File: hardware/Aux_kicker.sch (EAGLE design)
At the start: 23 parts, among them IC1 PIC18F4431S, IC2 MIC4429M, IC3 LM324D, Q1 IRF520

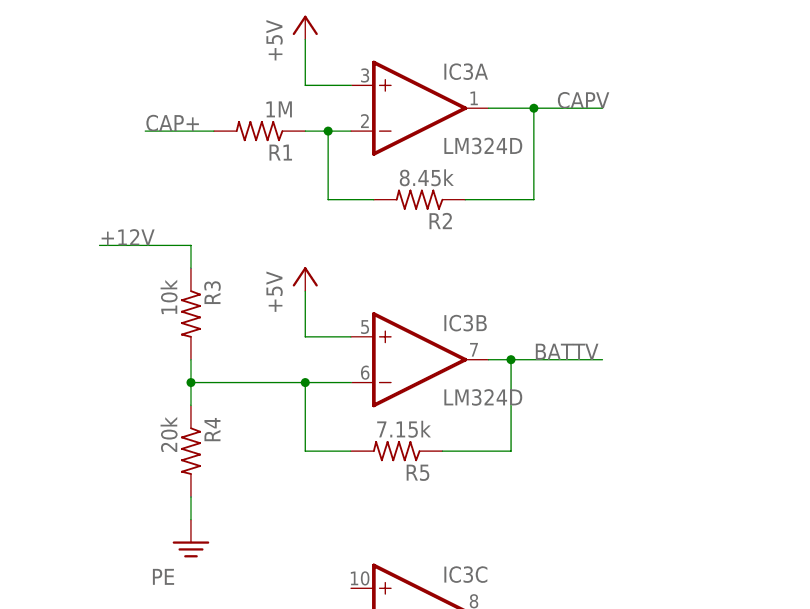
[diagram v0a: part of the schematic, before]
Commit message: Minor resistance value changes to aux kicker board
Changed values of resistances in op amp circuit to reflect ones used on
aux kicker boards with new 250V capacitors (instead of 500V capacitors)
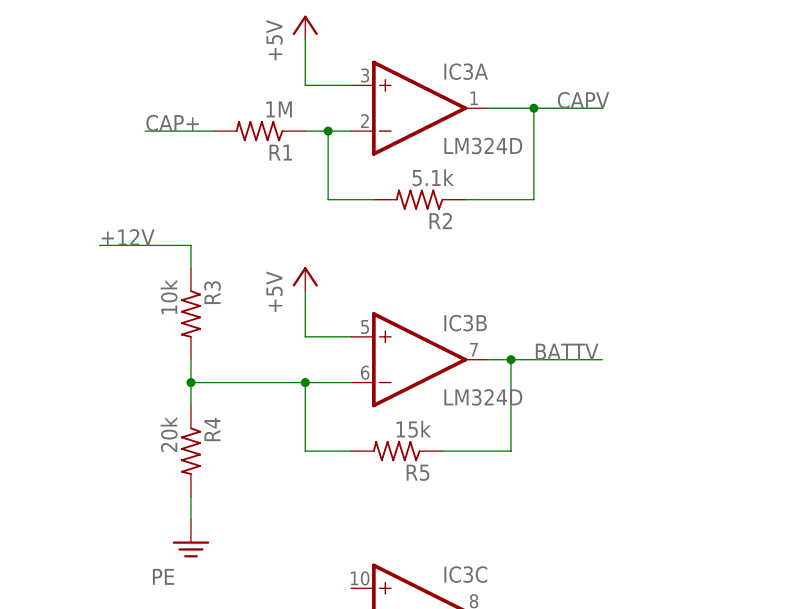
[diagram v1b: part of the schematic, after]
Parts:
- R2: value 8.45k -> 5.1k
- R5: value 7.15k -> 15k
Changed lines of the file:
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@@
 <part name="R1" library="rcl" deviceset="R-US_" device="R0805" value="1M"/>
 <part name="P+7" library="supply1" deviceset="+5V" device=""/>
-<part name="R2" library="rcl" deviceset="R-US_" device="R0805" value="8.45k"/>
+<part name="R2" library="rcl" deviceset="R-US_" device="R0805" value="5.1k"/>
 <part name="R3" library="rcl" deviceset="R-US_" device="R0805" value="10k"/>
 <part name="R4" library="rcl" deviceset="R-US_" device="R0805" value="20k"/>
 <part name="SUPPLY3" library="supply2" deviceset="PE" device=""/>
 <part name="P+11" library="supply1" deviceset="+5V" device=""/>
-<part name="R5" library="rcl" deviceset="R-US_" device="R0805" value="7.15k"/>
+<part name="R5" library="rcl" deviceset="R-US_" device="R0805" value="15k"/>
 </parts>
 <sheets>
